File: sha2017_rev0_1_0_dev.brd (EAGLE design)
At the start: 95 x 86 mm, 201 parts, among them IC1 CP210X_USB_UART, IC2 AP7215, IC3 ESP32WROOM32, IC4 MCP73833, IC5 FXL6408, IC6 CPT112, Q2 MMBT2222A, Q3 MMBT2222A, Q4 MMBT2222A, Q5 MMBT2222A, Q6 SI1304 BDL, Q7 MMBT2222A, T1 SI2301DS, T2 SI2301DS, T3 SI2301DS, X1 2908-05WB-MG, X3 JST-PH3

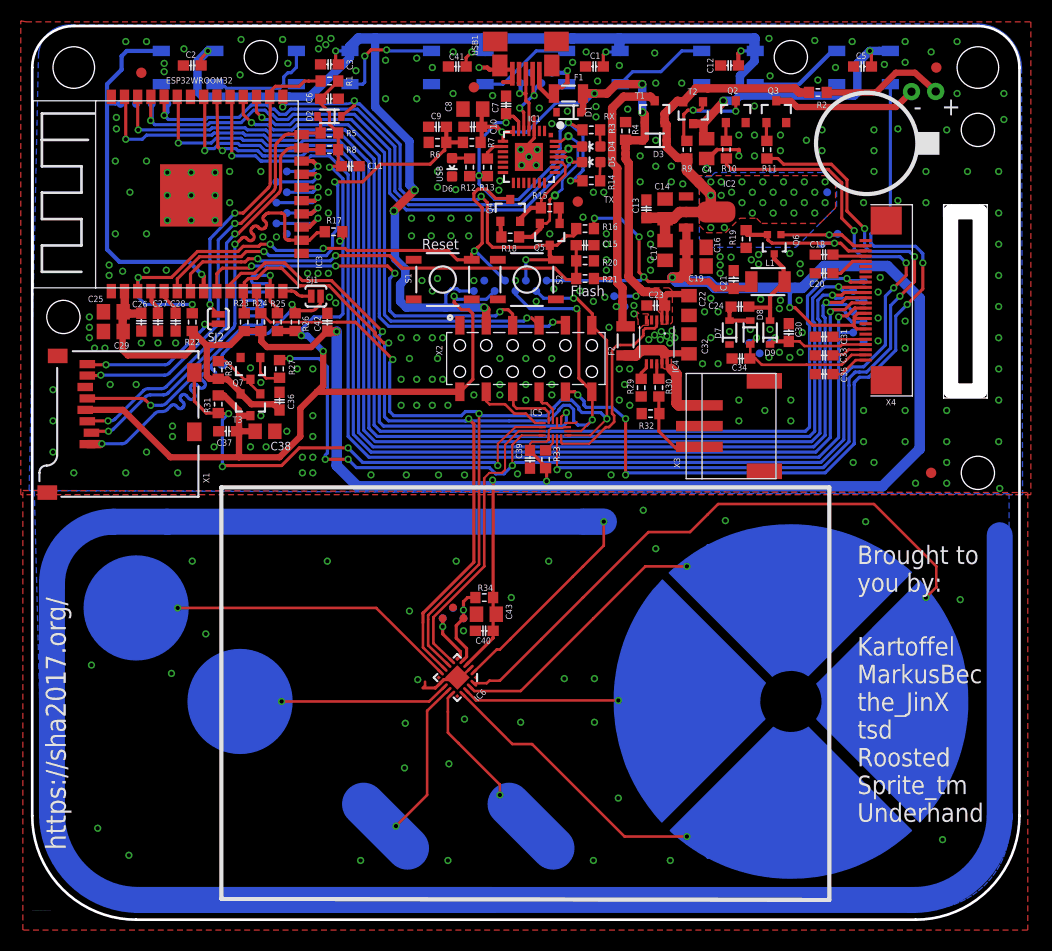
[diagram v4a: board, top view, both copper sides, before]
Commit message: fixing broken ground plane
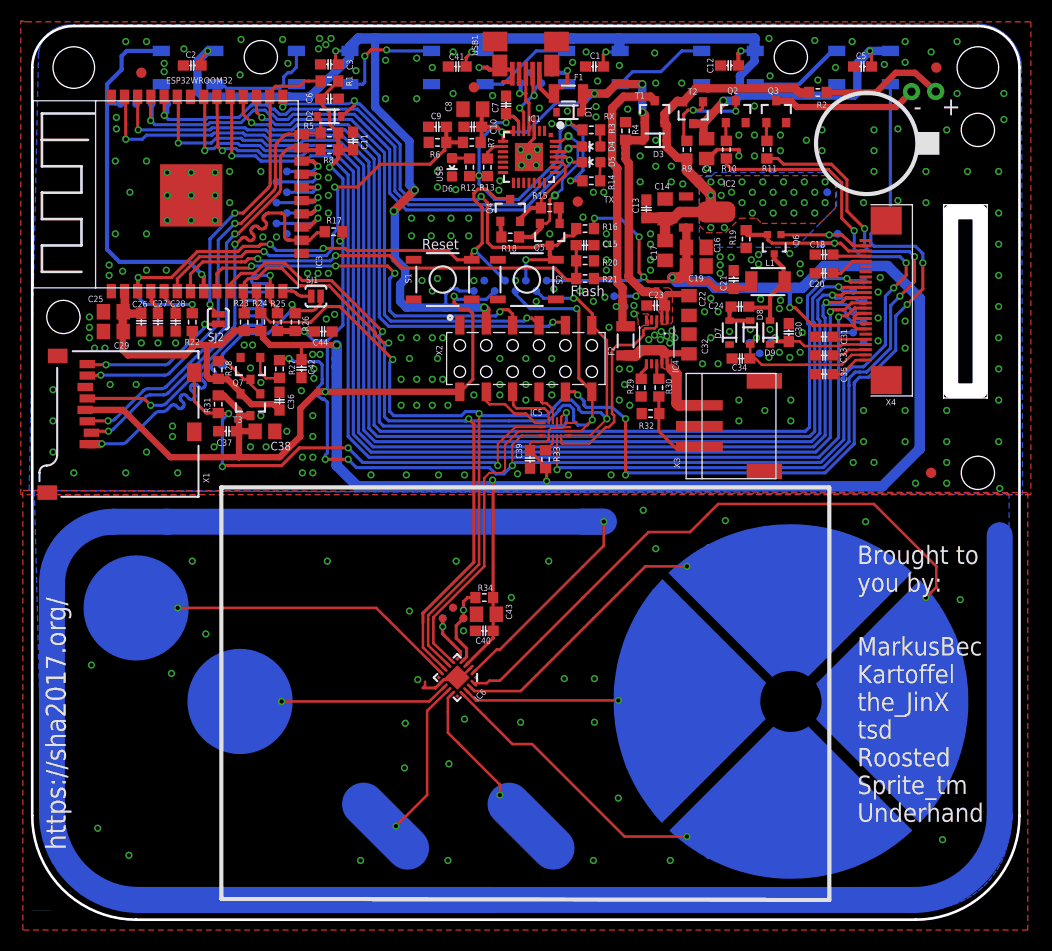
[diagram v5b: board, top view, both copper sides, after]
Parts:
- added C44: 100n, sha2017_rev0_1_0_dev:C0603-DASHES
- moved C42 5.11 mm to (25.9, 52.0), turned to 270 degrees
- moved C11 2.45 mm to (30.9, 73.9), turned to 90 degrees
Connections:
- net 3V3_SWITCHED: now also C44.1
- net GND: now also C44.2
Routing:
- net 3V3_SWITCHED: track 110.0 -> 112.9 mm
- net +3V3: track 239.1 -> 240.8 mm
- net I2C_SCL: track 94.3 -> 95.5 mm
- net VUSB_SENSE: track 40.6 -> 39.9 mm
- net GND: vias 297 -> 303
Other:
- board text added: "MarkusBec Kartoffel the_JinX tsd Roosted Sprite_tm Underhand"
- board text removed: "Kartoffel MarkusBec the_JinX tsd Roosted Sprite_tm Underhand"

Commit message: add some color
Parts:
- removed Q7: MMBT2222A, SparkFun-DiscreteSemi:SOT23-3
- removed TP5: TEST-POINT3, SparkFun-Passives:PAD.03X.03
- removed U$23, U$24, U$25: VIA, badge:VIA
- added $$U$4, $$U$5, $$U$6: VIA, badge:VIA
- added Q1: MMBT2222A, SparkFun-DiscreteSemi:SOT23-3
- added TP140: TEST-POINT3, SparkFun-Passives:PAD.03X.03
- C13, C15, C26, C41, C9: value 100n -> 4u7/16V; device sha2017_rev0_1_0_dev:C0603-DASHES -> rcl:C0805
- C14, C16, C22, C29, C4, C8: value 4u7/16V -> 100n; device rcl:C0805 -> sha2017_rev0_1_0_dev:C0603-DASHES
- C18, C20, C24, C30, C34: value 1u -> 4u7/16V; device sha2017_rev0_1_0_dev:C0603-DASHES -> rcl:C0805
- C19, C25, C32, C38: value 4u7/16V -> 1u; device rcl:C0805 -> sha2017_rev0_1_0_dev:C0603-DASHES
- C21, C39: value 100n -> 1u
- C31: value 1u -> 100n
- Q5: value MMBT2222A -> SI1304 BDL; device SparkFun-DiscreteSemi:SOT23-3 -> SparkFun-DiscreteSemi:SOT323
- Q6: value SI1304 BDL -> MMBT2222A; device SparkFun-DiscreteSemi:SOT323 -> SparkFun-DiscreteSemi:SOT23-3
- X1: value 2908-05WB-MG -> (none); device con-3m:MICRO-SD-SOCKET-PP -> EAGLE-FPC_CONNECTOR_AND_FFC_CAB-rev1:68712414022
- X2: value (none) -> 2908-05WB-MG; device EAGLE-BOARD-TO-BOARD_CONNECTORS-rev16c:610X12243021 -> con-3m:MICRO-SD-SOCKET-PP
- X3: value JST-PH3 -> (none); device badge:JST-PH3 -> EAGLE-BOARD-TO-BOARD_CONNECTORS-rev16c:610X12243021
- X4: value (none) -> JST-PH3; device EAGLE-FPC_CONNECTOR_AND_FFC_CAB-rev1:68712414022 -> badge:JST-PH3
- moved C30 65.0 mm to (7.80, 55.6), turned to 180 degrees
- moved X1 65.0 mm to (80.8, 58.6)
- moved C25 60.3 mm to (68.1, 58.0), turned to 0 degrees
- moved C38 54.1 mm to (76.2, 51.5)
- moved TP128 53.0 mm to (23.5, 68.0)
- moved TP124 53.0 mm to (77.5, 65.0)
- moved U$17 52.2 mm to (87.6, 6.70)
- moved TP129 52.0 mm to (76.5, 69.0)
- moved Q6 51.8 mm to (21.0, 52.1)
- moved C6 51.4 mm to (79.9, 81.1)
- moved $$U$8 48.4 mm to (54.1, 22.2)
- moved C31 48.2 mm to (28.0, 55.6)
- moved U$20 47.6 mm to (40.0, 4.70)
- moved U$18 47.4 mm to (9.30, 5.20)
- moved U$21 44.7 mm to (54.0, 4.70)
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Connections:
- net +3V3: now also C17.1, C20.1, C22.1, C27.1, C30.1, C37.1, C44.1, TP119.P$1, X1.10, X1.7, X1.9; no longer C16.1, C19.1, C21.1, C25.1, C29.1, C36.1, C40.1, TP118.P$1, X4.10, X4.7, X4.9
- net +5V: now also C11.1, C24.1, C9.1, TP112.P$1; no longer C10.1, C22.1, C8.1, TP111.P$1
- net 3V3_SWITCHED: now also C12.1, C31.1, C40.1, C41.1, C7.1, TP116.P$1, X2.4, X3.12; no longer C11.1, C37.1, C38.1, C44.1, C6.1, TP115.P$1, X1.4, X2.12
- net CD0: now also TP131.P$1; no longer TP130.P$1
- net CLK: now also TP130.P$1; no longer TP129.P$1
- net CND: now also TP128.P$1; no longer TP127.P$1
- net ESP32_!RESET: now also Q3.3, TP121.P$1; no longer Q4.3, TP120.P$1
- net ESP32_FLASH: now also Q4.3, TP120.P$1; no longer Q5.3, TP119.P$1
- net EXTIO-0: now also X3.3; no longer X2.3
- net EXTIO-1: now also X3.4; no longer X2.4
- net EXTIO-2: now also X3.5; no longer X2.5
- net EXTIO-3: now also X3.9; no longer X2.9
- net EXTIO-4: now also X3.10; no longer X2.10
- net EXTIO-5: now also X3.11; no longer X2.11
- net GDR: now also Q5.1, TP124.P$1, X1.23; no longer Q6.1, TP123.P$1, X4.23
- net GND: now also $$U$4.P$1, $$U$5.P$1, $$U$6.P$1, C12.2, C18.2, C19.1, C20.2, C21.1, C24.2, C27.2, C29.1, C30.2, C31.2, C32.1, C34.2, C36.1, C38.1, C4.1, C41.2, C6.1, Q1.2, Q6.2, TP1.P$1, TP106.P$1, TP122.P$1, TP125.P$1, TP140.P$1, X1.17, X1.8, X2.6, X2.CD2, X2.GND1, X2.GND3, X3.1, X4.2; no longer C12.1, C18.1, C19.2, C20.1, C21.2, C25.2, C27.1, C29.2, C30.1, C31.1, C32.2, C34.1, C36.2, C38.2, C4.2, C41.1, C6.2, Q3.2, Q7.2, TP121.P$1, TP124.P$1, TP139.P$1, TP3.P$1, TP5.P$1, U$23.P$1, U$24.P$1, U$25.P$1, X1.6, X1.CD2, X1.GND1, X1.GND3, X2.1, X3.2, X4.17, X4.8
- net I2C_SCL: now also TP114.P$1, X3.6; no longer TP113.P$1, X2.6
- net I2C_SDA: now also TP115.P$1, X3.7; no longer TP114.P$1, X2.7
- net LCD_!RESET: now also TP113.P$1, X1.15; no longer TP112.P$1, X4.15
- net LCD_BUSY: now also TP118.P$1, X1.16; no longer TP117.P$1, X4.16
- net LCD_CS: now also TP109.P$1, X1.13; no longer TP108.P$1, X4.13
- net LCD_D/!S: now also TP111.P$1, X1.14; no longer TP110.P$1, X4.14
- net LCD_MOSI: now also TP107.P$1, X1.11; no longer TP106.P$1, X4.11
- net LCD_SCK: now also TP108.P$1, X1.12; no longer TP107.P$1, X4.12
- net N$10: now also Q3.2; no longer Q4.2
- net N$11: now also Q4.2; no longer Q5.2
- net N$13: now also Q4.1; no longer Q5.1
- net N$14: now also Q3.1; no longer Q4.1
- net N$15: now also Q6.1; no longer Q7.1
- net N$16: now also Q2.3; no longer Q3.3
- net N$17: now also Q6.3; no longer Q7.3
- net N$22: now also C25.1; no longer C24.1
- net N$23: now also C25.2, Q5.3; no longer C24.2, Q6.3
- net N$3: now also D104.2; no longer D105.2
- net N$32: now also TP139.P$1; no longer TP136.P$1
- net N$4: now also D104.4, D105.2; no longer D104.2, D105.4
- net N$42: now also C28.2; no longer C27.2
- net N$43: now also C29.2; no longer C28.2
- net N$45: now also Q2.1; no longer Q3.1
- net N$48: now also X4.1; no longer X3.1
- net N$49: now also C34.1, X4.3; no longer C32.1, X3.3
- net N$52: now also Q1.1; no longer Q2.1
- net N$53: now also Q1.3; no longer Q2.3
- net N$6: now also X2.8; no longer X1.8
- net N$61: now also TP3.P$1; no longer TP2.P$1
- net N$62: now also TP2.P$1; no longer TP1.P$1
- net PREVGH: now also C32.2, X1.4; no longer C30.2, X4.4
- net PREVGL: now also C36.2, X1.2; no longer C34.2, X4.2
- net RESE: now also Q5.2, TP123.P$1, X1.22; no longer Q6.2, TP122.P$1, X4.22
- net SD1: now also TP132.P$1; no longer TP131.P$1
- net SD2: now also TP126.P$1; no longer TP125.P$1
- net SD3: now also TP127.P$1; no longer TP126.P$1
- net SD_CD: now also X2.CD1; no longer X1.CD1
- net SD_CLK: now also X2.5; no longer X1.5
- net SD_CMD: now also X2.3; no longer X1.3
- net SD_DATA0: now also X2.7; no longer X1.7
- net SD_DATA2_OUT: now also X2.1; no longer X1.1
- net SD_DATA3: now also X2.2; no longer X1.2
- net TSCL: now also X1.19; no longer X4.19
- net TSDA: now also X1.18; no longer X4.18
- net VBAT: now also TP110.P$1; no longer TP109.P$1
- net VBAT_SENSE: now also C16.1; no longer C15.1
- net VCC: now also C15.1, C18.1, TP129.P$1; no longer C13.1, C17.1, TP128.P$1
- net VCOM: now also C38.2, X1.1; no longer C35.2, X4.1
- net VDD: now also C8.1; no longer C7.1
- net VGH: now also C21.2, X1.20; no longer C20.2, X4.20
- net VGL: now also C19.2, X1.21; no longer C18.2, X4.21
- net VPP: now also X1.6; no longer X4.6
- net VSH: now also C33.2, X1.5; no longer C31.2, X4.5
- net VSL: now also C35.2, X1.3; no longer C33.2, X4.3
- net VUSB_SENSE: now also C10.1; no longer C9.1
- net WS2812_DATA: now also D105.4, TP136.P$1; no longer D104.4, TP132.P$1
- net WS2812_DATA_OUT: now also X3.8; no longer X2.8
- net WS2812_POWER: now also C13.1, C4.2, C6.2, TP117.P$1, X3.2; no longer C12.2, C4.1, C41.2, TP116.P$1, X2.2
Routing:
- net GND: vias 303 -> 304
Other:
- board text added: "Do not Touch"
- board text added: "Warning Radiation"
- board text removed: "/home/niek/Sync/Projects/SHA2017-badge/diyart-1bit.bmp"

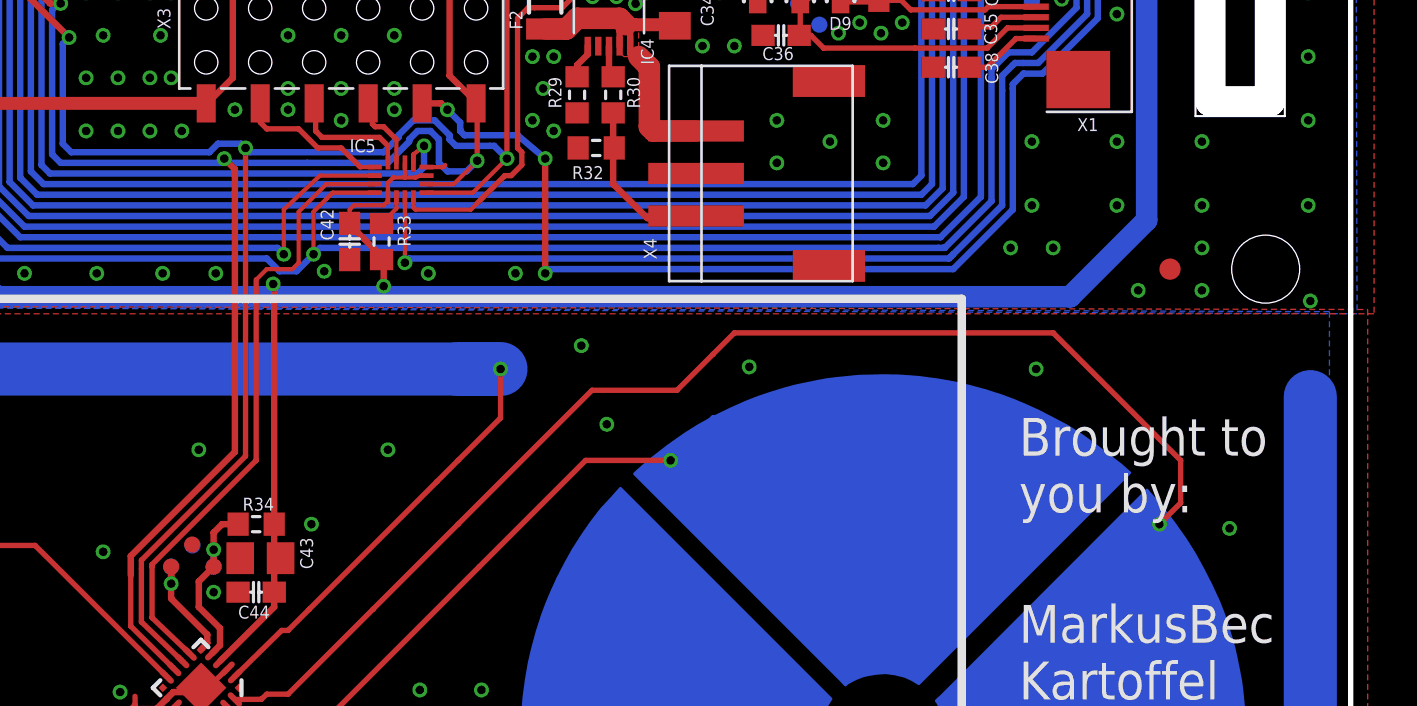
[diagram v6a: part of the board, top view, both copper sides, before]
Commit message: add missin ground via at cpt112 programming interface
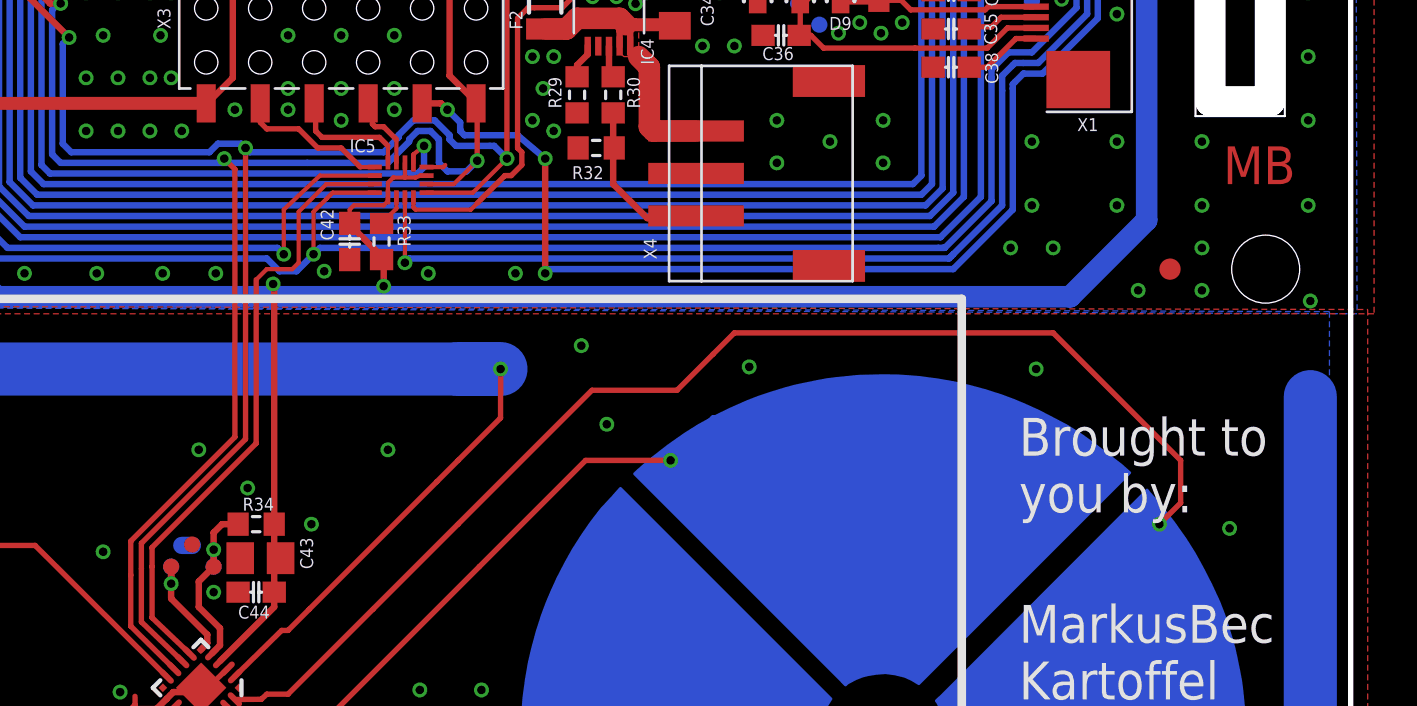
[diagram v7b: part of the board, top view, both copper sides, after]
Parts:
- added U$23: VIA, badge:VIA
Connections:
- net GND: now also U$23.P$1
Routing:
- net GND: track 19.1 -> 19.6 mm
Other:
- board text added: "MB"
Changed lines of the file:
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@@
 <setting verticaltext="up"/>
 </settings>
-<grid distance="1" unitdist="mm" unit="mm" style="lines" multiple="1" display="yes" altdistance="0.025" altunitdist="inch" altunit="inch"/>
+<grid distance="0.1" unitdist="mm" unit="mm" style="lines" multiple="1" display="yes" altdistance="0.025" altunitdist="inch" altunit="inch"/>
 <layers>
 <layer number="1" name="Top" color="4" fill="1" visible="yes" active="yes"/>
@@
 <layer number="21" name="tPlace" color="7" fill="1" visible="yes" active="yes"/>
 <layer number="22" name="bPlace" color="7" fill="1" visible="yes" active="yes"/>
-<layer number="23" name="tOrigins" color="15" fill="1" visible="no" active="yes"/>
-<layer number="24" name="bOrigins" color="15" fill="1" visible="no" active="yes"/>
+<layer number="23" name="tOrigins" color="15" fill="1" visible="yes" active="yes"/>
+<layer number="24" name="bOrigins" color="15" fill="1" visible="yes" active="yes"/>
 <layer number="25" name="tNames" color="7" fill="1" visible="yes" active="yes"/>
 <layer number="26" name="bNames" color="7" fill="1" visible="yes" active="yes"/>
@@
 <text x="86" y="0" size="1.778" layer="22" font="vector" ratio="15" rot="MR0">Do not Touch</text>
 <text x="5" y="52" size="1.778" layer="22" font="vector" ratio="15" rot="MR90">Warning Radiation </text>
+<text x="89" y="46" size="1.778" layer="1" font="vector" ratio="15">MB</text>
 </plain>
 <attributes>
@@
 <attribute name="VALUE" x="27.2" y="53.95" size="1.016" layer="27"/>
 </element>
+<element name="U$23" library="badge" package="VIA" value="VIA" x="43.1" y="31.7">
+<attribute name="PARTNO" value="NAP" x="43.1" y="31.7" size="1.778" layer="27" font="vector" ratio="15" display="off"/>
+</element>
 </elements>
 <signals>
@@
 <via x="28.5" y="70.4" extent="1-16" drill="0.4"/>
 <via x="22.9" y="65.1" extent="1-16" drill="0.4"/>
-<wire x1="40.49" y1="29.04" x2="40.5" y2="29" width="0" layer="19" extent="1-16"/>
+<wire x1="40.5" y1="29" x2="40" y2="29" width="0.8128" layer="16"/>
+<contactref element="U$23" pad="P$1"/>
+<wire x1="40.5" y1="29" x2="40.49" y2="29.04" width="0" layer="19" extent="1-16"/>
 </signal>
 <signal name="USB_DN_CON">
@@
 <wire x1="40.37118125" y1="23.911028125" x2="38.6" y2="25.6" width="0.254" layer="1"/>
 <wire x1="38.6" y1="25.6" x2="38.6" y2="28" width="0.254" layer="1"/>
-<wire x1="38.6" y1="28" x2="38.6" y2="28.1" width="0.254" layer="1"/>
+<wire x1="38.6" y1="28" x2="38.6" y2="28.9" width="0.254" layer="1"/>
 <contactref element="IC5" pad="7"/>
 <wire x1="49.0815" y1="46" x2="46.8" y2="46" width="0.2" layer="1"/>
@@
 <wire x1="45.2" y1="42" x2="44" y2="42" width="0.2" layer="1"/>
 <wire x1="44" y1="42" x2="43.5" y2="41.5" width="0.2" layer="1"/>
-<wire x1="43.5" y1="41.5" x2="43.5" y2="33" width="0.254" layer="1"/>
-<wire x1="43.5" y1="33" x2="38.6" y2="28.1" width="0.254" layer="1"/>
+<wire x1="43.5" y1="41.5" x2="43.5" y2="33.8" width="0.254" layer="1"/>
+<wire x1="43.5" y1="33.8" x2="38.6" y2="28.9" width="0.254" layer="1"/>
 </signal>
 <signal name="I2C_SDA">
@@
 <wire x1="52.5" y1="46.6" x2="53.4" y2="46.6" width="0.3048" layer="16"/>
 <wire x1="53.4" y1="46.6" x2="53.9" y2="47.1" width="0.3048" layer="16"/>
-<wire x1="37.6" y1="27.6" x2="37.6" y2="28.5" width="0.3048" layer="1"/>
-<wire x1="37.6" y1="28.5" x2="42.5" y2="33.4" width="0.3048" layer="1"/>
-<wire x1="42.5" y1="33.4" x2="42.5" y2="46.7" width="0.3048" layer="1"/>
-<wire x1="42.5" y1="46.7" x2="42" y2="47.2" width="0.3048" layer="1"/>
+<wire x1="37.6" y1="27.6" x2="37.6" y2="29.2" width="0.254" layer="1"/>
+<wire x1="37.6" y1="29.2" x2="42.5" y2="34.1" width="0.254" layer="1"/>
+<wire x1="42.5" y1="34.1" x2="42.5" y2="46.7" width="0.254" layer="1"/>
+<wire x1="42.5" y1="46.7" x2="42" y2="47.2" width="0.254" layer="1"/>
 <via x="42" y="47.2" extent="1-16" drill="0.4"/>
 <wire x1="42" y1="47.2" x2="41.9" y2="47.2" width="0.3048" layer="16"/>
@@
 <via x="55.3" y="47.2" extent="1-16" drill="0.4"/>
 <wire x1="55.3" y1="47.2" x2="53.7" y2="45.6" width="0.2" layer="1"/>
-<wire x1="38.1" y1="27.9" x2="38.1" y2="28.3" width="0.254" layer="1"/>
-<wire x1="38.1" y1="28.3" x2="43" y2="33.2" width="0.254" layer="1"/>
-<wire x1="43" y1="33.2" x2="43" y2="47.7" width="0.254" layer="1"/>
+<wire x1="38.1" y1="27.9" x2="38.1" y2="29.1" width="0.254" layer="1"/>
+<wire x1="38.1" y1="29.1" x2="43" y2="34" width="0.254" layer="1"/>
+<wire x1="43" y1="34" x2="43" y2="47.7" width="0.254" layer="1"/>
 <via x="43" y="47.7" extent="1-16" drill="0.4"/>
 <wire x1="49.5" y1="47.5" x2="43.2" y2="47.5" width="0.3048" layer="16"/>
